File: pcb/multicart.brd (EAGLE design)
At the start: 63.5 x 88.3 mm, 20 parts, among them IC1 27C64-27C080, IC2 74HCT373N, IC3 74HCT08N, Q1 BS170

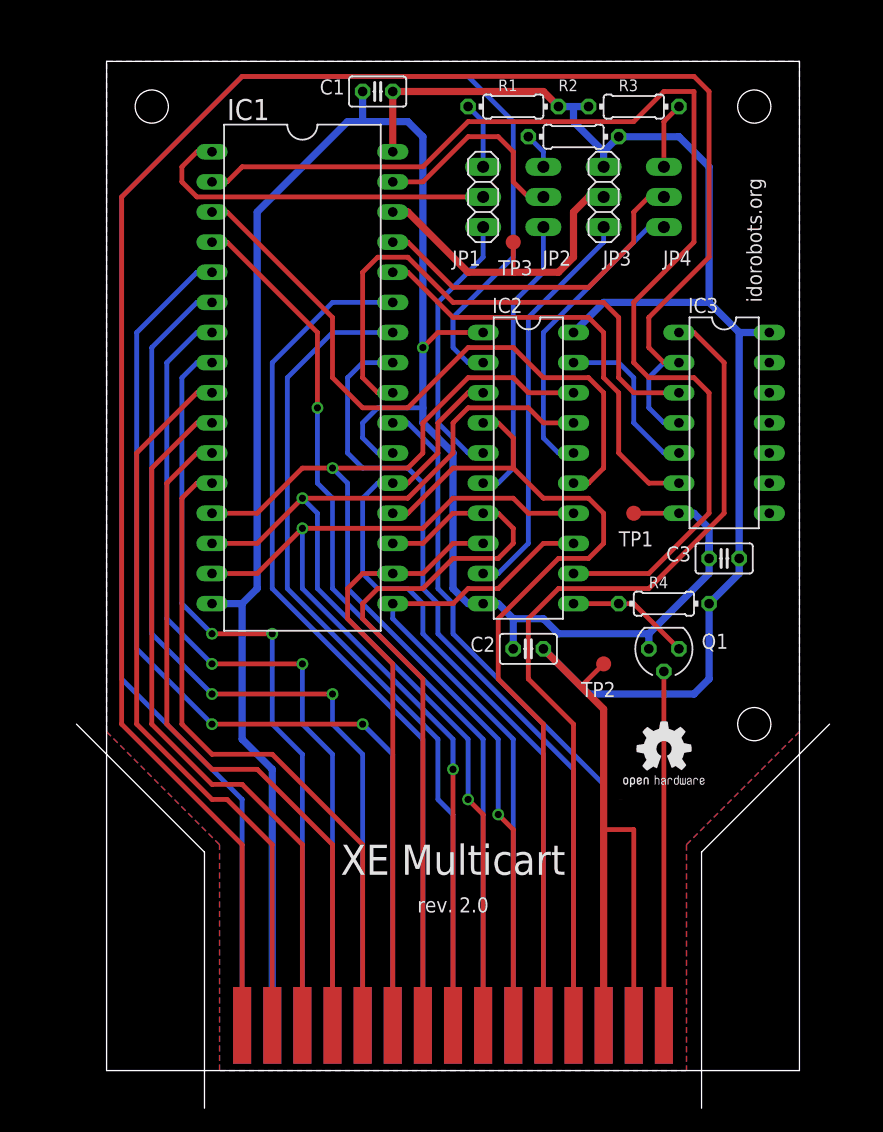
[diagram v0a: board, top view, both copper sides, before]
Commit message: Updated the design to fit into a Z7 cart case.
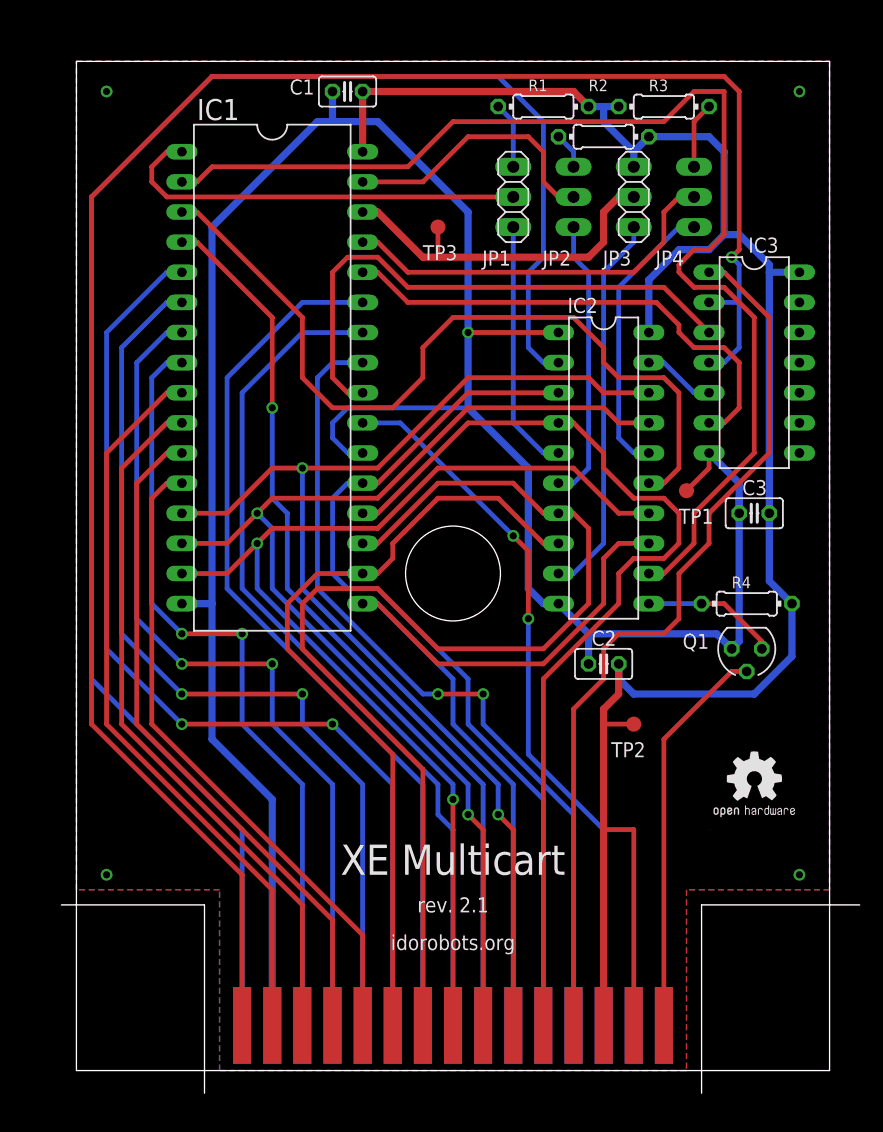
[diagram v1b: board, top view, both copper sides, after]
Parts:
- moved GOLD_ORB_SM1 8.03 mm to (55.9, 17.8)
- moved Q1 6.98 mm to (59.1, 33.0)
- moved R4 6.98 mm to (59.1, 36.8)
- moved C2 6.48 mm to (47.0, 31.8)
- moved TP3 6.48 mm to (33.0, 68.6)
- moved IC2 6.35 mm to (47.0, 48.3)
- moved IC3 5.68 mm to (59.7, 57.1)
- moved TP2 5.68 mm to (49.5, 26.7)
- moved TP1 4.84 mm to (54.0, 46.4)
- moved C3 4.58 mm to (59.7, 44.5)
- moved JP2 2.54 mm to (44.5, 71.1)
- moved C1 2.54 mm to (25.4, 80.0)
- moved IC1 2.54 mm to (19.1, 55.9)
- moved JP1 2.54 mm to (39.4, 71.1)
- moved JP3 2.54 mm to (49.5, 71.1)
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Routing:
- net D5: track 65.5 -> 97.2 mm
- net D3: track 57.1 -> 74.2 mm
- net GND: track 188.6 -> 205.5 mm
- net D4: track 51.4 -> 68.1 mm
- net N$3: track 55.9 -> 69.2 mm
- net D2: track 80.8 -> 92.1 mm
- net D0: track 90.5 -> 99.0 mm
- net D7: track 67.6 -> 76.0 mm
- net N$1: track 14.3 -> 6.13 mm
- net D1: track 88.0 -> 95.7 mm
- net D6: track 76.5 -> 83.1 mm
- net N$21: track 36.7 -> 42.2 mm
- net N$10: track 17.9 -> 23.0 mm
- net N$13: track 30.3 -> 35.3 mm
- net N$22: track 137.1 -> 141.6 mm
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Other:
- board size 63.5 x 88.3 mm -> 67.3 x 87 mm
- board text added: "rev. 2.1"
- board text removed: "rev. 2.0"

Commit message: Increased the via drill size.
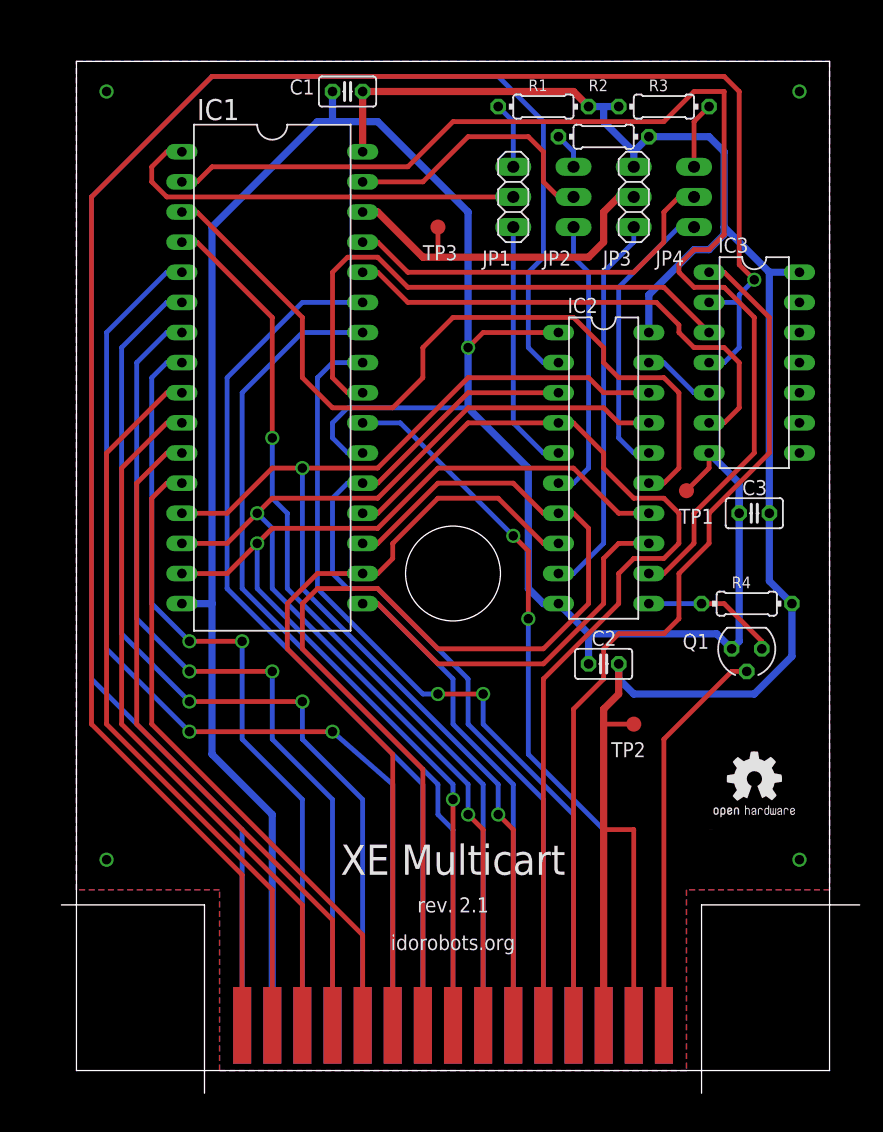
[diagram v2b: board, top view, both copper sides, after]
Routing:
- net VCC: track 172.9 -> 172.0 mm
- net GND: track 205.5 -> 206.1 mm
- net N$19: track 162.2 -> 162.7 mm

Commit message: Used proper alignment markers instead of vias.
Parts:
- added U$1, U$2, U$3, U$4, U$5, U$6, U$7, U$8: (no value), marks:PASSER-CIRCLE
- moved GOLD_ORB_SM1 2.84 mm to (54.6, 20.3)
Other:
- outline, holes or cut-outs redrawn
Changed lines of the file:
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@@
 <text x="34.29" y="11.43" size="1.27" layer="21" font="vector" rot="R180" align="center">rev. 2.1</text>
 <wire x1="2.54" y1="82.55" x2="66.04" y2="82.55" width="0" layer="20"/>
-<wire x1="66.04" y1="82.55" x2="66.04" y2="-2.54" width="0" layer="20"/>
-<wire x1="66.04" y1="-2.54" x2="2.54" y2="-2.54" width="0" layer="20"/>
-<wire x1="2.54" y1="-2.54" x2="2.54" y2="82.55" width="0" layer="20"/>
+<wire x1="66.04" y1="82.55" x2="66.04" y2="-3.175" width="0" layer="20"/>
+<wire x1="66.04" y1="-3.175" x2="2.54" y2="-3.175" width="0" layer="20"/>
+<wire x1="2.54" y1="-3.175" x2="2.54" y2="82.55" width="0" layer="20"/>
 <wire x1="13.335" y1="-4.445" x2="13.335" y2="11.43" width="0" layer="46"/>
 <wire x1="13.335" y1="11.43" x2="1.27" y2="11.43" width="0" layer="46"/>
@@
 <attribute name="VALUE" x="36.195" y="74.93" size="1.27" layer="27" rot="R270"/>
 </element>
-<element name="GOLD_ORB_SM1" library="bfl" package="OSHW2" value="OSHWLOGO_GOLD_ORB_SM" x="55.88" y="17.78"/>
+<element name="GOLD_ORB_SM1" library="bfl" package="OSHW2" value="OSHWLOGO_GOLD_ORB_SM" x="54.61" y="20.32"/>
 <element name="TP1" library="testpad" package="B1,27" value="TPB1,27" x="53.975" y="46.355" smashed="yes">
 <attribute name="TP_SIGNAL_NAME" value="GND" x="53.34" y="44.45" size="1" layer="37" display="off"/>
@@
 <attribute name="VALUE" x="32.385" y="67.818" size="0.0254" layer="27"/>
 </element>
+<element name="U$1" library="marks" package="PASSER-CIRCLE" value="" x="6.35" y="78.74"/>
+<element name="U$2" library="marks" package="PASSER-CIRCLE" value="" x="62.23" y="78.74"/>
+<element name="U$3" library="marks" package="PASSER-CIRCLE" value="" x="62.23" y="78.74" rot="MR180"/>
+<element name="U$4" library="marks" package="PASSER-CIRCLE" value="" x="6.35" y="78.74" rot="MR180"/>
+<element name="U$5" library="marks" package="PASSER-CIRCLE" value="" x="6.35" y="15.24" rot="MR180"/>
+<element name="U$6" library="marks" package="PASSER-CIRCLE" value="" x="6.35" y="15.24" rot="R180"/>
+<element name="U$7" library="marks" package="PASSER-CIRCLE" value="" x="62.23" y="15.24" rot="R180"/>
+<element name="U$8" library="marks" package="PASSER-CIRCLE" value="" x="62.23" y="15.24" rot="MR180"/>
 </elements>
 <signals>
@@
 <vertex x="66.04" y="12.7"/>
 <vertex x="53.975" y="12.7"/>
-<vertex x="53.975" y="-2.54"/>
-<vertex x="14.605" y="-2.54"/>
+<vertex x="53.975" y="-3.175"/>
+<vertex x="14.605" y="-3.175"/>
 <vertex x="14.605" y="12.7"/>
 <vertex x="2.54" y="12.7"/>
@@
 <vertex x="66.04" y="12.7"/>
 <vertex x="53.975" y="12.7"/>
-<vertex x="53.975" y="-2.54"/>
-<vertex x="14.605" y="-2.54"/>
+<vertex x="53.975" y="-3.175"/>
+<vertex x="14.605" y="-3.175"/>
 <vertex x="14.605" y="12.7"/>
 <vertex x="2.54" y="12.7"/>
@@
 <wire x1="39.37" y1="68.58" x2="39.37" y2="52.07" width="0.4064" layer="16"/>
 </signal>
-<signal name="N$17">
-<via x="5.08" y="80.01" extent="1-16" drill="0.8" shape="octagon"/>
-</signal>
-<signal name="N$20">
-<via x="63.5" y="80.01" extent="1-16" drill="0.8" shape="octagon"/>
-</signal>
-<signal name="N$23">
-<via x="63.5" y="15.24" extent="1-16" drill="0.8" shape="octagon"/>
-</signal>
-<signal name="N$24">
-<via x="5.08" y="15.24" extent="1-16" drill="0.8" shape="octagon"/>
-</signal>
 </signals>

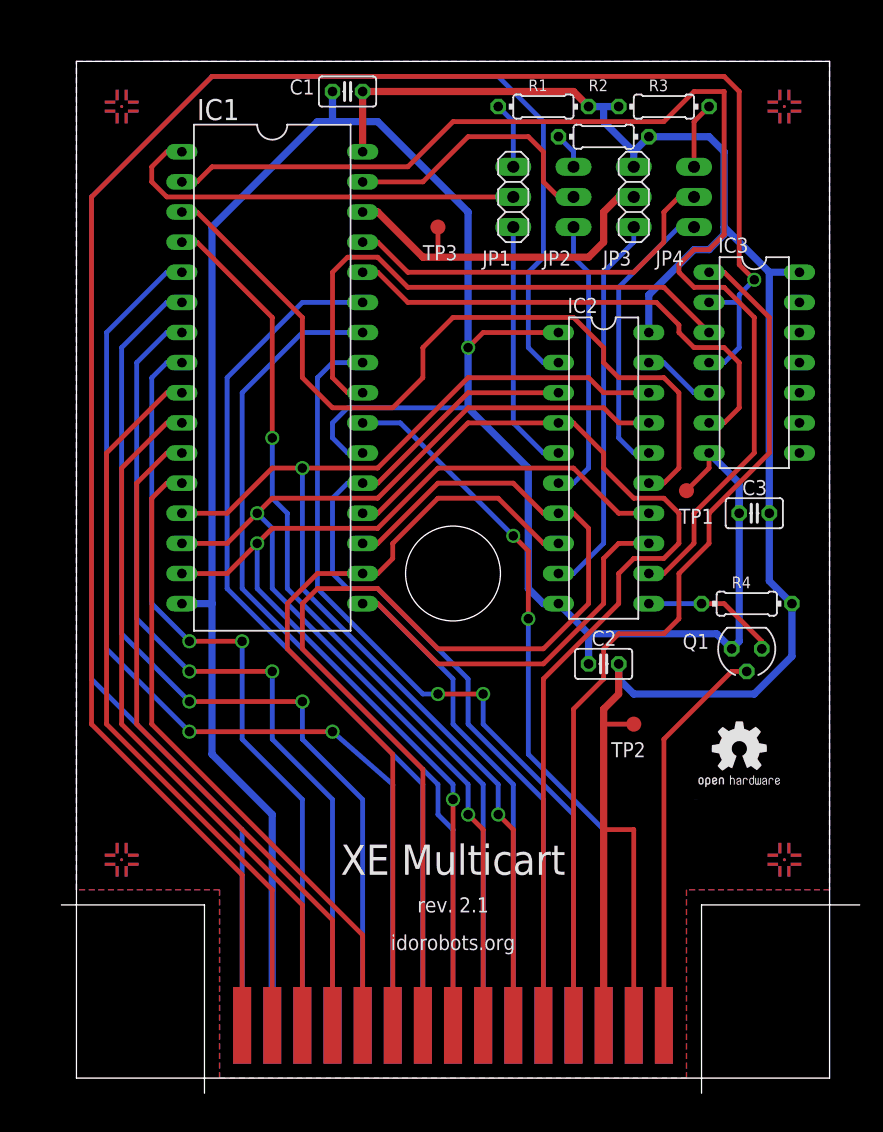
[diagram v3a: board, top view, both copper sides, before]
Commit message: Optimized the design.
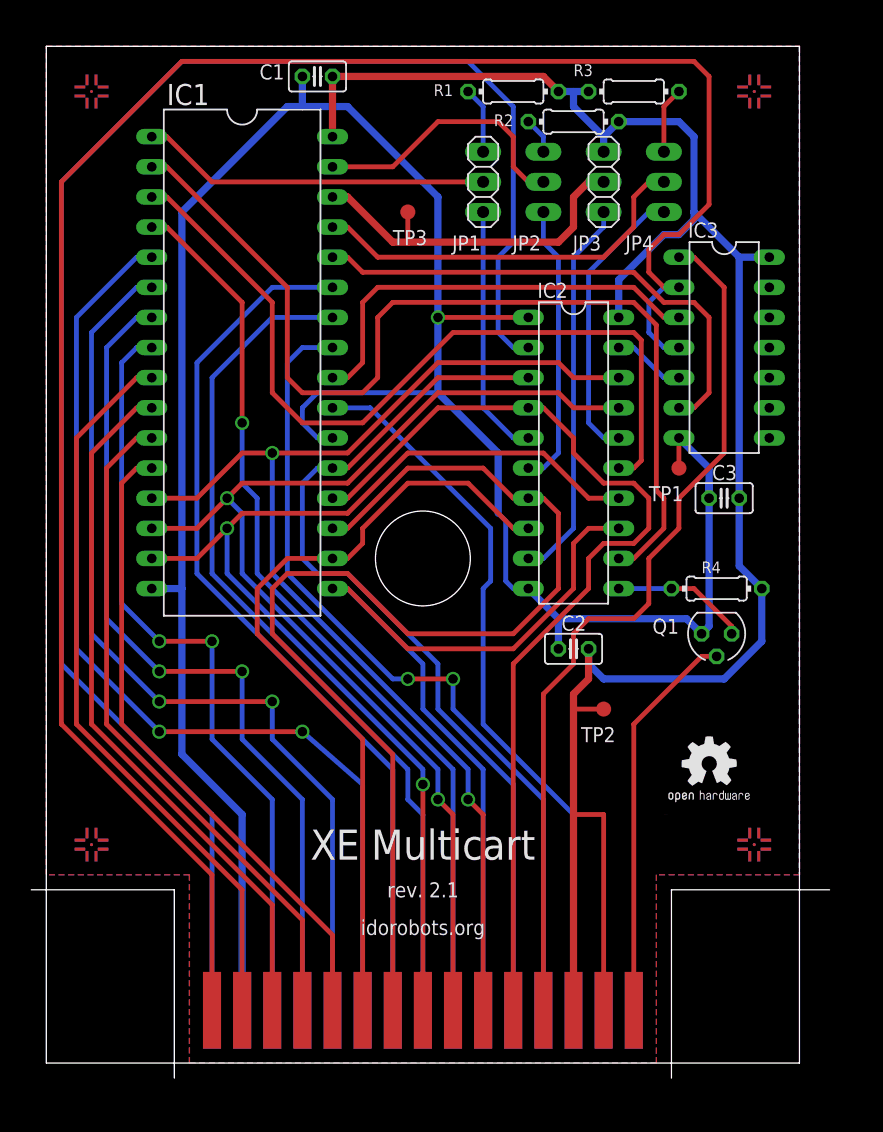
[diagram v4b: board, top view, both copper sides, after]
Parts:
- moved U$1 2.84 mm to (3.81, 80.0)
- moved U$4 2.84 mm to (3.81, 80.0)
- moved JP2 2.84 mm to (41.9, 72.4)
- moved R1 2.84 mm to (39.4, 80.0)
- moved R3 2.84 mm to (49.5, 80.0)
- moved U$2 2.84 mm to (59.7, 80.0)
- moved U$3 2.84 mm to (59.7, 80.0)
- moved C2 2.84 mm to (44.5, 33.0)
- moved IC2 2.84 mm to (44.5, 49.5)
- moved IC3 2.84 mm to (57.1, 58.4)
- moved R4 2.84 mm to (56.5, 38.1)
- moved TP3 2.84 mm to (30.5, 69.8)
- moved U$5 2.84 mm to (3.81, 16.5)
- moved U$6 2.84 mm to (3.81, 16.5)
- moved U$7 2.84 mm to (59.7, 16.5)
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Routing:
- net N$4: track 100.4 -> 84.1 mm
- net N$27: track 46.9 -> 36.4 mm
- net N$13: track 35.3 -> 29.5 mm
- net N$19: track 162.7 -> 165.6 mm, vias 1 -> 0
- net GND: track 206.1 -> 204.1 mm
- net N$21: track 42.2 -> 43.3 mm
- net N$18: track 75.4 -> 74.4 mm
- net A10: track 61.1 -> 61.6 mm, vias 2 -> 0

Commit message: Moved the board to match the origin.
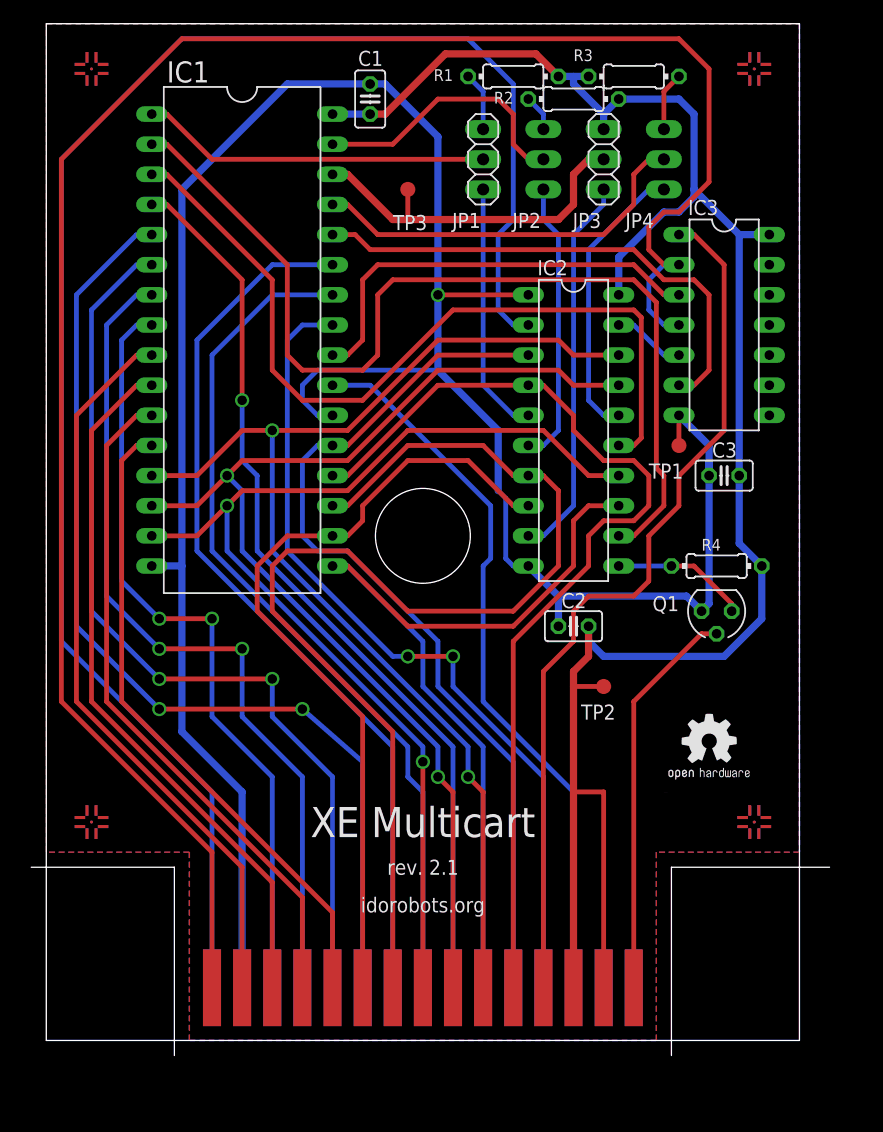
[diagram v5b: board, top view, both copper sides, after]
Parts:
- moved C1 4.84 mm to (27.3, 79.4), turned to 90 degrees
- moved C3 1.91 mm to (57.1, 47.6)
- moved IC1 1.91 mm to (16.5, 59.1)
- moved IC2 1.91 mm to (44.5, 51.4)
- moved IC3 1.91 mm to (57.1, 60.3)
- moved JP1 1.91 mm to (36.8, 74.3)
- moved JP2 1.91 mm to (41.9, 74.3)
- moved JP3 1.91 mm to (47.0, 74.3)
- moved JP4 1.91 mm to (52.1, 74.3)
- moved Q1 1.91 mm to (56.5, 36.2)
- moved R2 1.91 mm to (44.5, 79.4)
- moved R4 1.91 mm to (56.5, 40.0)
- moved TP1 1.91 mm to (53.3, 50.2)
- moved TP3 1.91 mm to (30.5, 71.8)
- moved U$1 1.91 mm to (3.81, 81.9)
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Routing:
- net VCC: track 172.0 -> 168.7 mm
- net N$19: track 165.6 -> 164.8 mm
- net GND: track 204.1 -> 203.4 mm
- net N$9: track 5.61 -> 4.97 mm
- net N$16: track 5.61 -> 4.97 mm

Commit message: Adjusted the board dimensions to better fit into a Z7 case.
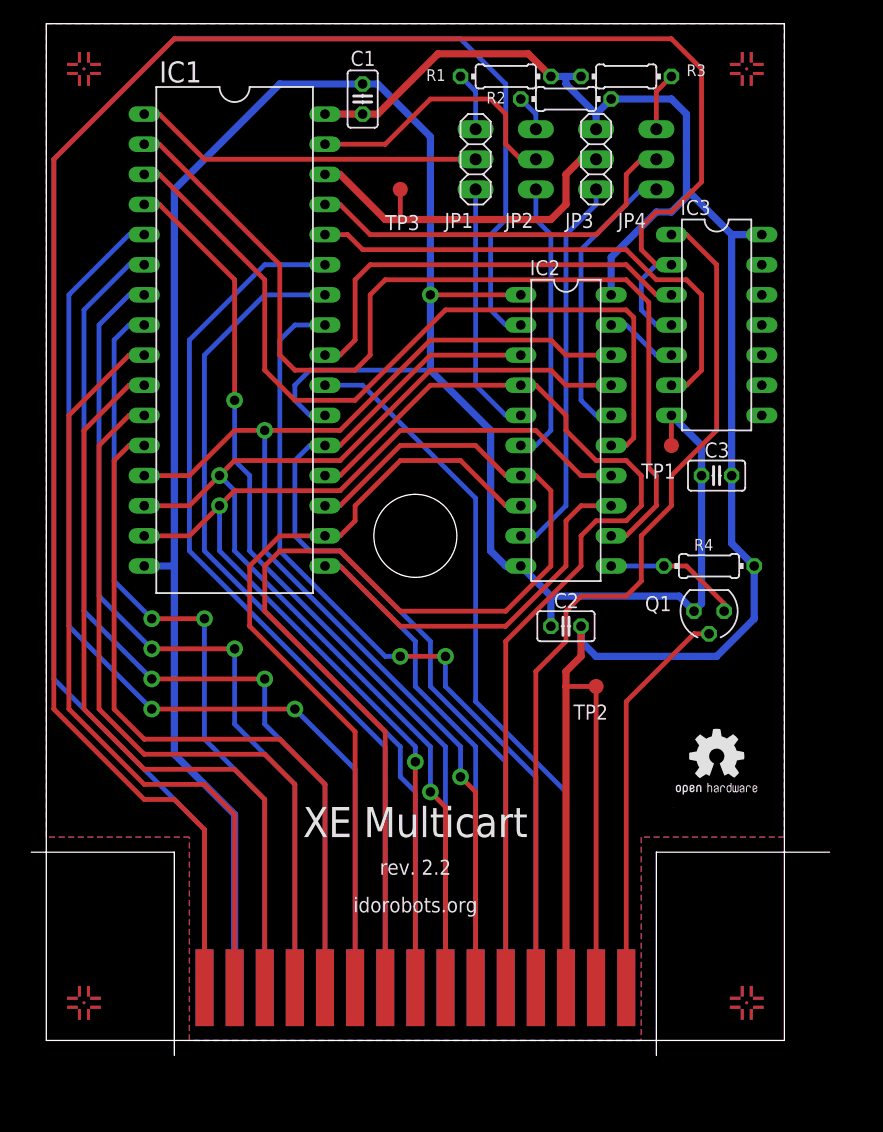
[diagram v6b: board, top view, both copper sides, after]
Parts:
- moved U$5 15.3 mm to (3.17, 3.17)
- moved U$6 15.3 mm to (3.17, 3.17)
- moved U$7 15.3 mm to (59.1, 3.17)
- moved U$8 15.3 mm to (59.1, 3.17)
- moved GOLD_ORB_SM1 1.42 mm to (52.7, 19.7)
- moved C2 0.64 mm to (43.8, 34.9)
- moved IC2 0.64 mm to (43.8, 51.4)
- moved JP3 0.64 mm to (46.4, 74.3)
- moved R2 0.64 mm to (43.8, 79.4)
- moved TP1 0.64 mm to (52.7, 50.2)
- moved TP2 0.64 mm to (46.4, 29.8)
- moved IC1 0.64 mm to (15.9, 59.1)
- moved J1 0.64 mm to (31.1, 0.64)
- moved TP3 0.64 mm to (29.8, 71.8)
- moved U$1 0.64 mm to (3.17, 81.9)
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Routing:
- net A0: track 54.9 -> 61.6 mm
- net VCC: track 168.7 -> 175.0 mm
- net A1: track 57.4 -> 63.4 mm
- net A2: track 60.0 -> 64.4 mm
- net A3: track 62.5 -> 65.5 mm
- net N$19: track 164.8 -> 166.3 mm
- net A10: track 61.6 -> 61.1 mm
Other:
- outline, holes or cut-outs redrawn
- board text added: "rev. 2.2"
- board text removed: "rev. 2.1"
